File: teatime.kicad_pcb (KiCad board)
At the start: 2 copper layers, 52 x 30.5 mm, 33 parts, among them J1 I2C, J2 UPDI, SW3 C&K PTS526, SW4 C&K PTS526, U1 GoodDisplay_GDC04212, U2 ATtiny417-M, Y1 32.768kHz 12.5pF

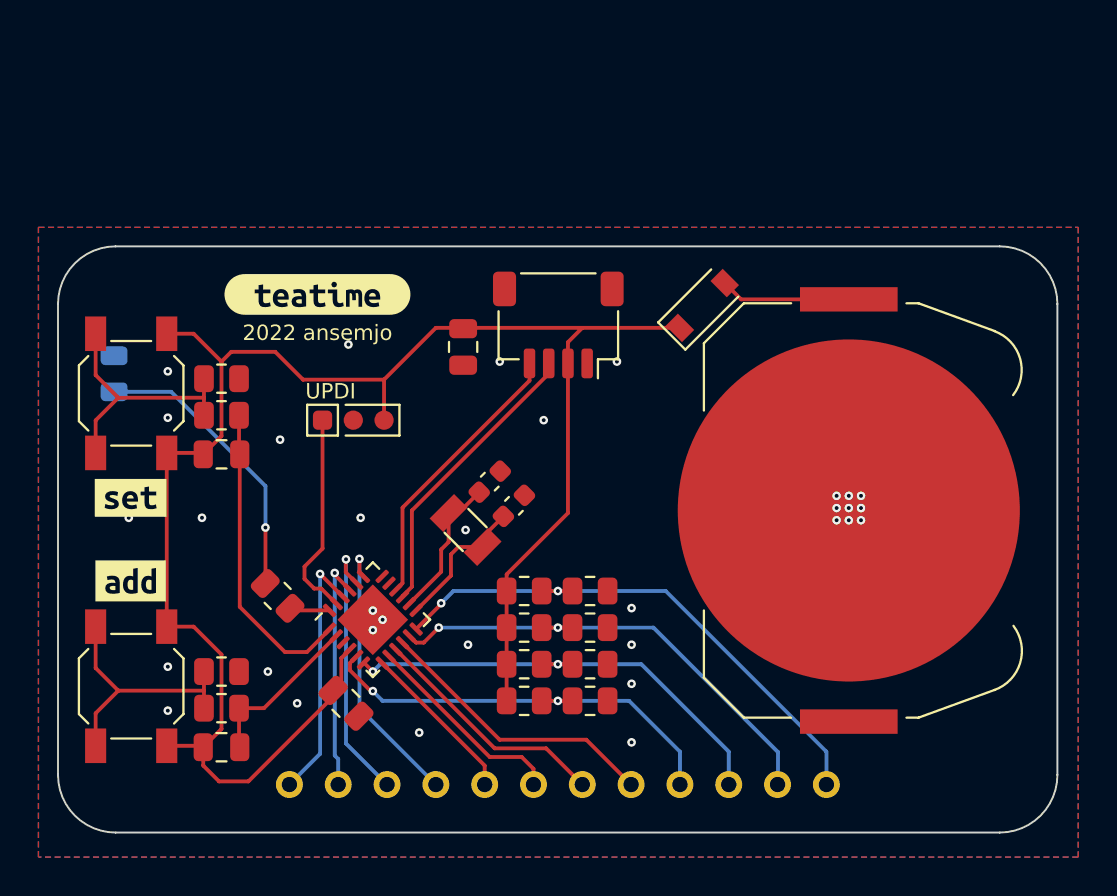
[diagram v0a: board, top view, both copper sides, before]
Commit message: updated design using dedicated rohm BU9796AMUV driver
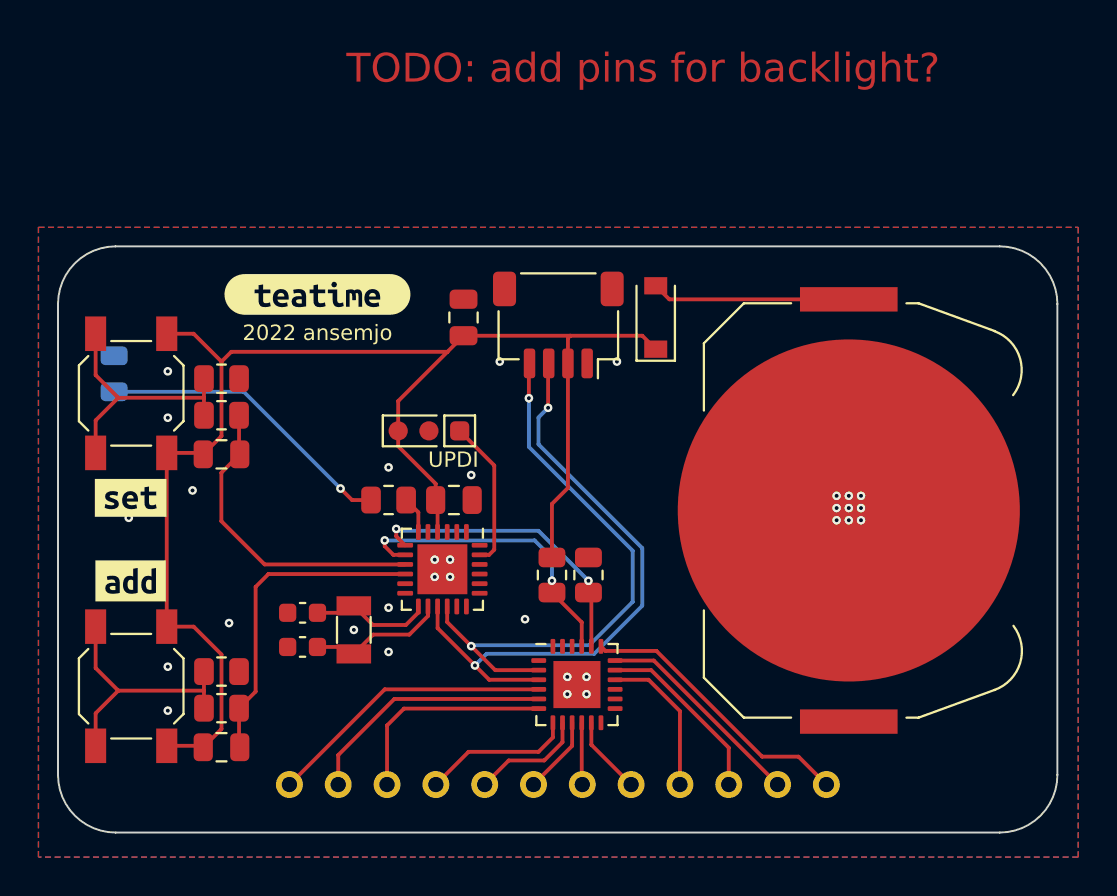
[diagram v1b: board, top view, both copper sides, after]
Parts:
- removed R10, R11, R12, R13, R8, R9: 470kΩ, Resistor_SMD:R_0805_2012Metric
- added U3: BU9796AMUV, Package_DFN_QFN:VQFN-24-1EP_4x4mm_P0.5mm_EP2.45x2.45mm, F.Cu at (125.3, 91.1)
- R6, R7: value 470kΩ -> DNP
- moved C5 13.0 mm to (111.0, 89.1), turned to 180 degrees
- moved C4 12.3 mm to (111.0, 87.4), turned to 180 degrees
- moved C6 12.0 mm to (118.9, 81.5), turned to 0 degrees
- moved Y1 7.80 mm to (113.7, 88.3), turned to 90 degrees
- moved R5 7.63 mm to (115.5, 81.5), turned to 0 degrees
- moved U2 4.47 mm to (118.3, 85.1), turned to -90 degrees
- moved J2 3.97 mm to (117.6, 77.9), turned to 180 degrees
- moved D1 2.51 mm to (129.4, 72.0), turned to 90 degrees
- moved R6 1.67 mm to (124.0, 85.4), turned to -90 degrees
- moved C3 1.53 mm to (119.4, 72.0), turned to 90 degrees
- moved R7 0.84 mm to (125.9, 85.4), turned to 90 degrees
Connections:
- R6 pad 2: /com1 -> LCD_VDD
- R7 pad 1: /com1 -> LCD_VLCD
- U2 pad 1: BTN1 -> unconnected-(U2-Pad1)
- U2 pad 10: /1fgep -> BTN2
- U2 pad 11: /com2 -> unconnected-(U2-Pad11)
- U2 pad 12: /com1 -> unconnected-(U2-Pad12)
- U2 pad 19: /3fgep -> unconnected-(U2-Pad19)
- U2 pad 2: BTN2 -> unconnected-(U2-Pad2)
- U2 pad 20: /3abcd -> unconnected-(U2-Pad20)
- U2 pad 21: /4fgep -> unconnected-(U2-Pad21)
- U2 pad 22: /4abcd -> unconnected-(U2-Pad22)
- U2 pad 24: LED -> unconnected-(U2-Pad24)
- U2 pad 5: /com4 -> unconnected-(U2-Pad5)
- U2 pad 6: /com3 -> LED
- U2 pad 7: /2abcd -> LCD_VLCD
- U2 pad 8: /2fgep -> LCD_VDD
- U2 pad 9: /1abcd -> BTN1
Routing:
- net SDA: track 15.3 -> 32.6 mm, vias 0 -> 2
- net SCL: track 14.7 -> 30.6 mm, vias 0 -> 2
- net LCD_VDD: track 0.00 -> 15.9 mm, vias 0 -> 2
- net LCD_VLCD: track 0.00 -> 15.6 mm, vias 0 -> 2
- net /com4: track 23.1 -> 7.87 mm, vias 2 -> 0
- net /com3: track 24.5 -> 9.50 mm, vias 2 -> 0
- net VCC: track 91.9 -> 76.9 mm
- net /com2: track 25.6 -> 11.1 mm, vias 2 -> 0
- net /com1: track 29.0 -> 14.7 mm, vias 2 -> 0
- net /1fgep: track 14.9 -> 4.07 mm
- net /1abcd: track 12.6 -> 3.23 mm
- net BTN2: track 8.67 -> 16.8 mm
- net /2fgep: track 10.8 -> 4.05 mm
- net /3fgep: track 14.4 -> 7.87 mm, vias 1 -> 0
- net Net-(BT1-Pad1): track 6.81 -> 10.3 mm
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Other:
- board text added: "TODO: add pins for backlight?"

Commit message: rounded tracks
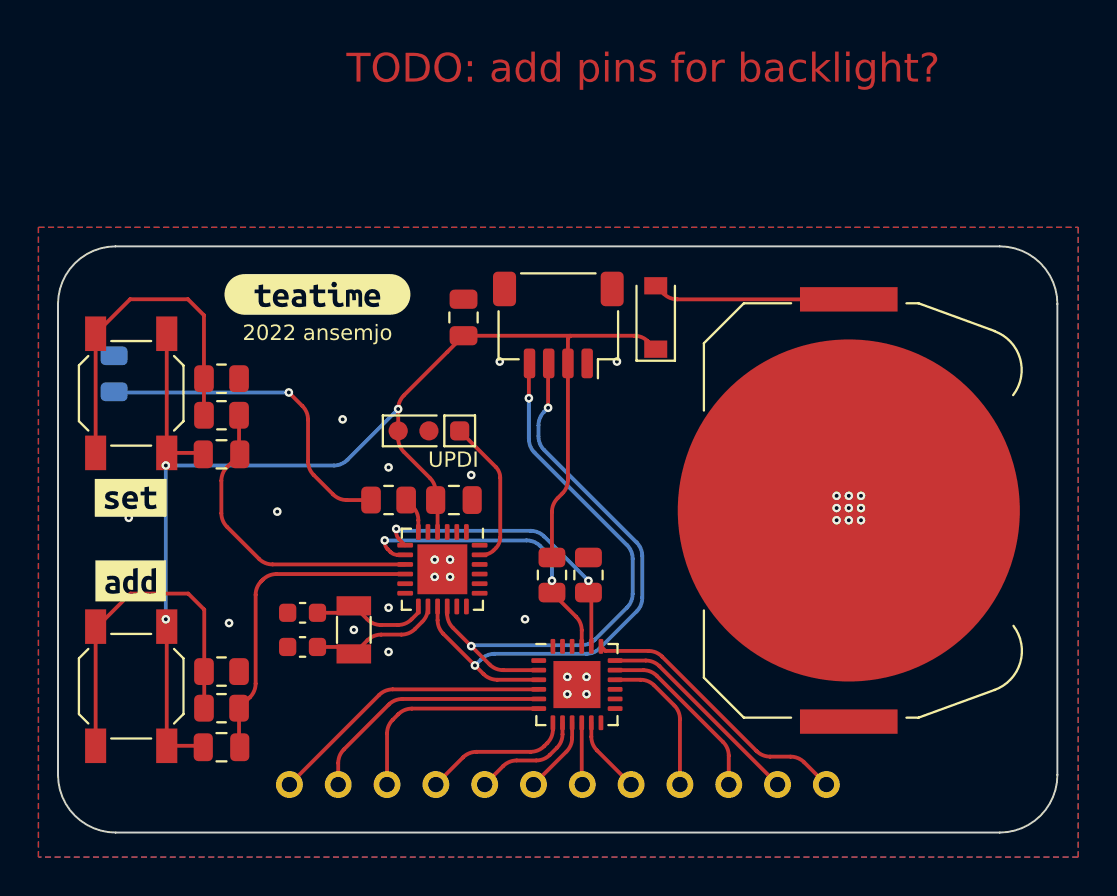
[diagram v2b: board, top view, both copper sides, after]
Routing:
- net Net-(R3-Pad1): track 13.5 -> 18.1 mm
- net Net-(R1-Pad1): track 13.5 -> 18.1 mm
- net VCC: track 76.9 -> 73.0 mm, vias 0 -> 3
- net Net-(D2-Pad2): track 15.7 -> 17.3 mm
- net GND: vias 32 -> 29
